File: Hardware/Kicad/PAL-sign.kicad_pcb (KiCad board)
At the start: 4 copper layers, 100 x 85 mm, 113 parts, among them J1 12402012E212A, J2 I2S, J3 FRONT, J4 VIDEO1, J5 VIDEO2, J6 VIDEO3, J7 Barrel_Jack_Switch, SW1 BOOT, U1 W25Q128JVS, U2 USBLC6-2P6, U3 RP2350A, U4 ADV7391BCPZ, U5 RV-3028-C7, U6 THS7314, U7 TPS62160DSG, U8 TPS7A2033PDBVR, U9 TPS7A2018PDBVR, Y1 ABM8-272-T3

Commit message: Update with ML2032 battery
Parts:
- removed the C21 at (189.4, 88.0)
- added BT1: ML2032, Library:CR2032-BS-6-1, F.Cu at (142.2, 99.8)
- renumbered C22 to C21, C23 to C22, C24 to C23, C25 to C24, C26 to C25, C27 to C26, C28 to C27, C29 to C28, C30 to C29, C31 to C30, C32 to C31, C33 to C32, C34 to C33, C35 to C34, C36 to C35, C37 to C36, C38 to C37, C39 to C38, C40 to C39, C41 to C40, C42 to C41, C43 to C42, C44 to C43, C45 to C44, C46 to C45, C47 to C46
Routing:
- net Net-(BT1-+): track 7.56 -> 53.5 mm, vias 0 -> 2
- net GND: track 62.6 -> 65.7 mm, vias 108 -> 109

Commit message: Update connector labels
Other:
- board text added: "3V3"
- board text added: "5V"
- board text added: "BCK"
- board text added: "DISPLAY+ROTARY"
- board text added: "DOUT"
- board text added: "D_BL"
- board text added: "D_CS"
- board text added: "D_DC"
- board text added: "D_MOSI"
- board text added: "D_RST"
- board text added: "D_SCK"
- board text added: "ENABLE"
- board text added: "GND"
- board text added: "LRCK"
- board text added: "PCM1808"
- board text added: "PUSH"
- board text added: "ROT_A"
- board text added: "ROT_B"
- board text added: "SCKI"

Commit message: Small hardware update
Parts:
- added C21: 100n, Capacitor_SMD:C_0603_1608Metric, F.Cu at (183.5, 89.2)
- moved C20 10.2 mm to (168.5, 100.8), turned to -90 degrees
- renumbered C22 to C20, C20 to C22, C21 to C23, C23 to C25, C25 to C26, C26 to C27, C27 to C28, C28 to C29, C29 to C30, C30 to C31, C31 to C32, C32 to C33, C33 to C34, C34 to C35, C35 to C36, C36 to C37, C37 to C38, C38 to C39, C39 to C40, C40 to C41, C41 to C42, C42 to C43, C43 to C44, C44 to C45, C45 to C46, C46 to C47
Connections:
- C20 pad 1: Net-(U4-P_{VDD}) -> +1V8
- C30 pad 2: +1V8 -> Net-(U4-P_{VDD})
- R19 pad 1: +1V8 -> Net-(U4-P_{VDD})
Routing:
- net Net-(U4-P_{VDD}): track 12.3 -> 18.7 mm
- net +1V8: track 84.3 -> 78.8 mm
- net GND: track 65.7 -> 69.0 mm, vias 109 -> 110
- net Net-(BT1-+): track 53.5 -> 55.3 mm

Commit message: Update PSU, so USB powering works too
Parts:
- removed R25: 10k, Resistor_SMD:R_0603_1608Metric
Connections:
- U7 pad 8: Net-(U7-PG) -> GND
- U8 pad 3: Net-(U7-PG) -> +5V
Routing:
- net Net-(U7-PG): track 20.7 -> 0.00 mm
- net +5V: track 130.1 -> 132.3 mm
- net GND: track 69.0 -> 69.8 mm, vias 110 -> 111

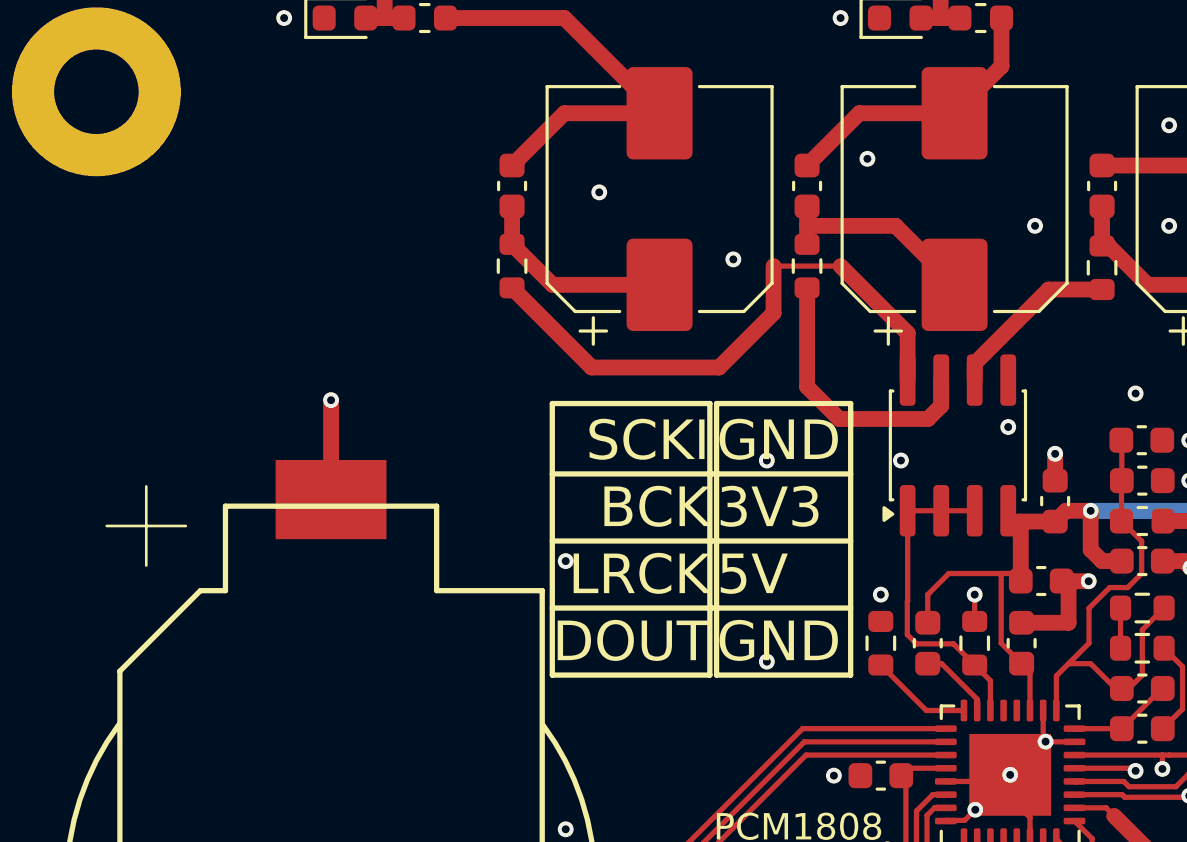
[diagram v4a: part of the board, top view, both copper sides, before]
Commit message: Hardware: series inductor for the DAC HF compensation
Add L3 (4.7 uH) and L4 (1.5 uH), both 0805, in series with R15: 6.2 uH
in total, chosen from measurements (4.7+2.2 was too high, 4.7+1.0 too
low). The two existing 1008 coils move to L5/L6. Gerbers, BOM,
positions, netlist and schematic PDF regenerated.
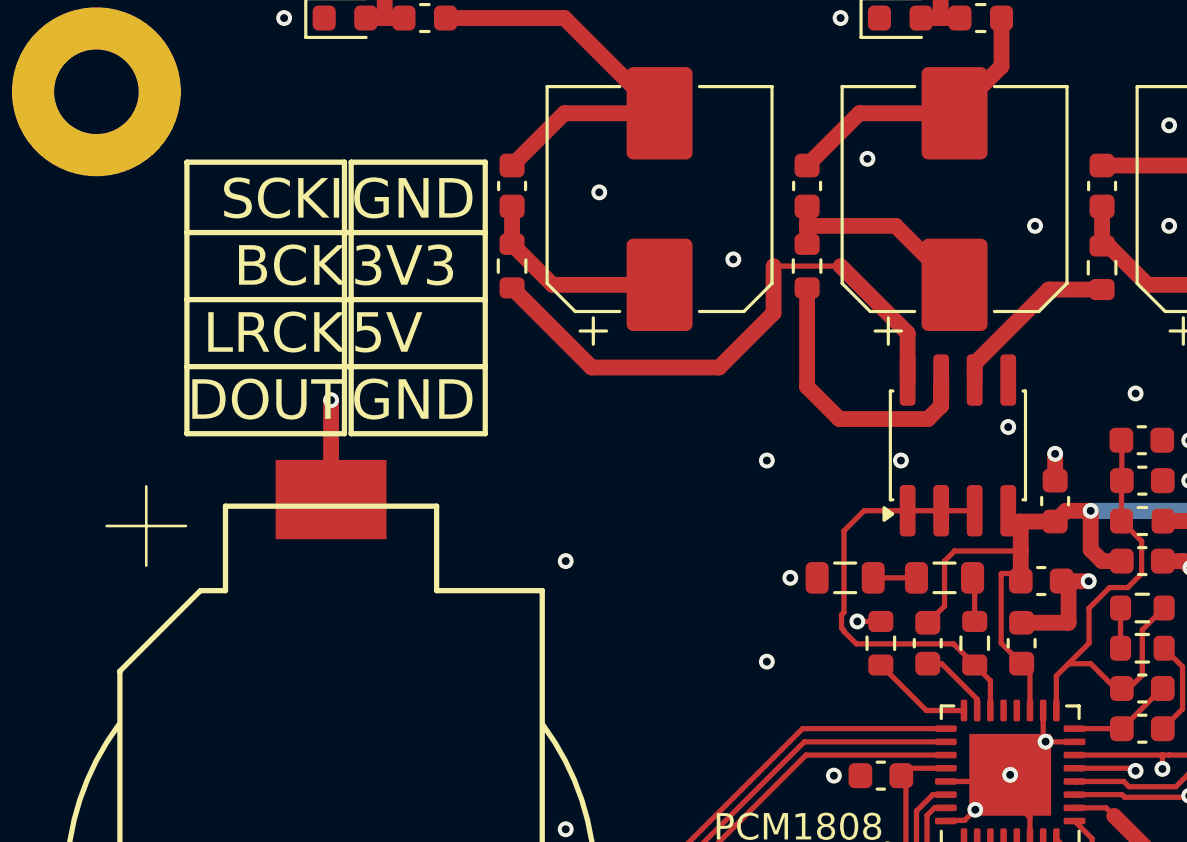
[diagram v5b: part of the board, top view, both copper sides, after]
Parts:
- added L3: 4.7uH, Inductor_SMD:L_0805_2012Metric, F.Cu at (165.5, 88.3)
- added L4: 1.5uH, Inductor_SMD:L_0805_2012Metric, F.Cu at (161.7, 88.3)
- renumbered L3 to L5, L4 to L6
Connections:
- R15 pad 2: GND -> Net-(L3-Pad1)
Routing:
- net Net-(U4-DAC1): track 12.2 -> 16.6 mm
- net Net-(L3-Pad1): track 0.00 -> 1.68 mm
- net Net-(L3-Pad2): track 0.00 -> 1.64 mm
- net +3.3VA: track 56.2 -> 57.7 mm
